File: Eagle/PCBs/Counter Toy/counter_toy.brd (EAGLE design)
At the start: 55.9 x 81.3 mm, 210 parts, among them Q100 2N7002, Q101 2N7002, Q102 2N7002, Q103 2N7002, Q104 2N7002, Q105 2N7002, Q106 2N7002, Q11 2N7002, Q12 2N7002, Q126 2N7002, Q127 2N7002, Q128 2N7002, Q129 2N7002, Q130 2N7002, Q131 2N7002, Q132 2N7002, Q133 2N7002, Q134 2N7002, Q135 2N7002, Q136 2N7002, Q137 2N7002, Q138 2N7002, Q139 2N7002, Q140 2N7002, Q141 2N7002, Q142 2N7002, Q162 2N7002, Q163 2N7002, Q164 2N7002, Q165 2N7002, Q166 2N7002, Q167 2N7002, Q168 2N7002, Q169 2N7002, Q170 2N7002, Q171 2N7002, Q172 2N7002, Q173 2N7002, Q174 2N7002, Q175 2N7002, Q176 2N7002, Q177 2N7002, Q178 2N7002, Q18 2N7002, Q19 2N7002, Q198 2N7002, Q199 2N7002, Q2 2N7002, Q20 2N7002, Q200 2N7002, Q201 2N7002, Q202 2N7002, Q203 2N7002, Q204 2N7002, Q205 2N7002, Q206 2N7002, Q207 2N7002, Q208 2N7002, Q209 2N7002, Q210 2N7002, Q211 2N7002, Q212 2N7002, Q213 2N7002, Q214 2N7002, Q24 2N7002, Q25 2N7002, Q26 2N7002, Q27 2N7002, Q28 2N7002, Q29 2N7002, Q30 2N7002, Q31 2N7002, Q32 2N7002, Q33 2N7002, Q34 2N7002, Q36 2N7002, Q37 2N7002, Q38 2N7002, Q39 2N7002, Q40 2N7002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

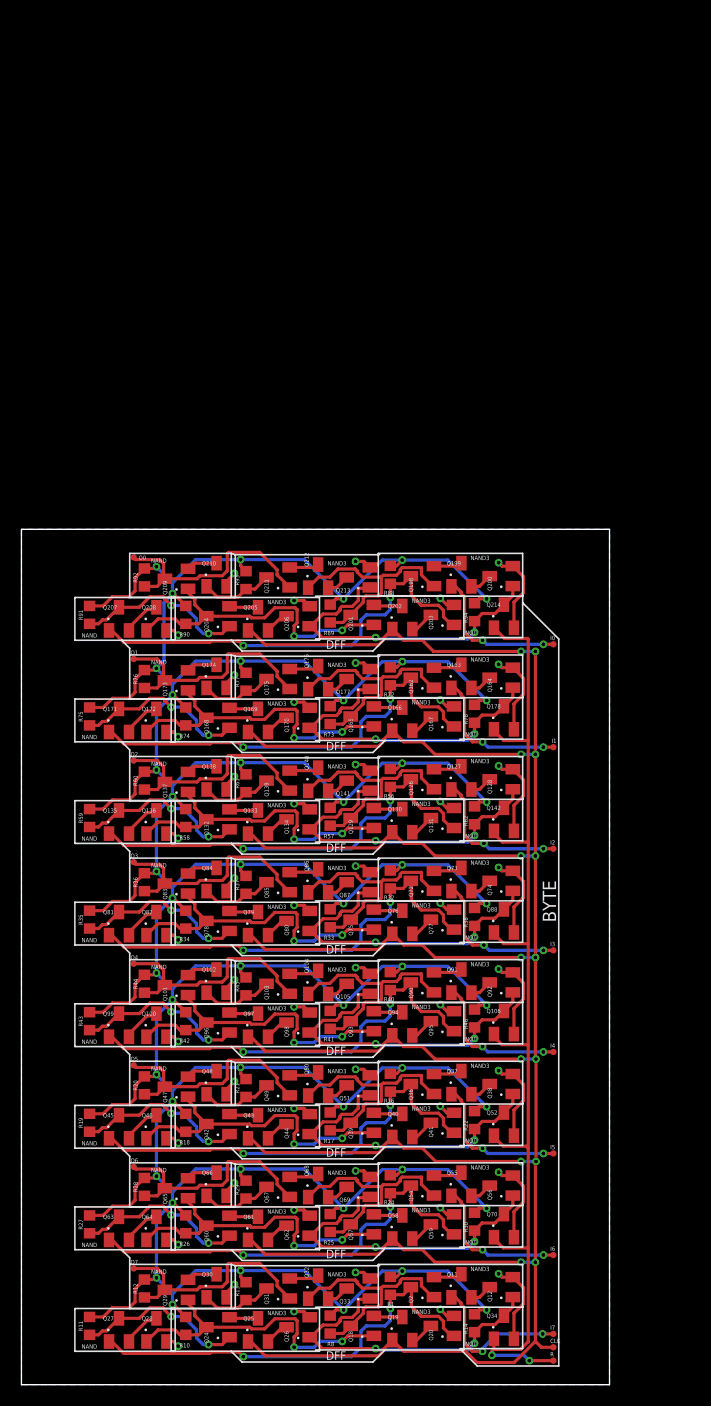
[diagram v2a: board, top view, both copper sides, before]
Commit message: Made a button input and a multiplexer
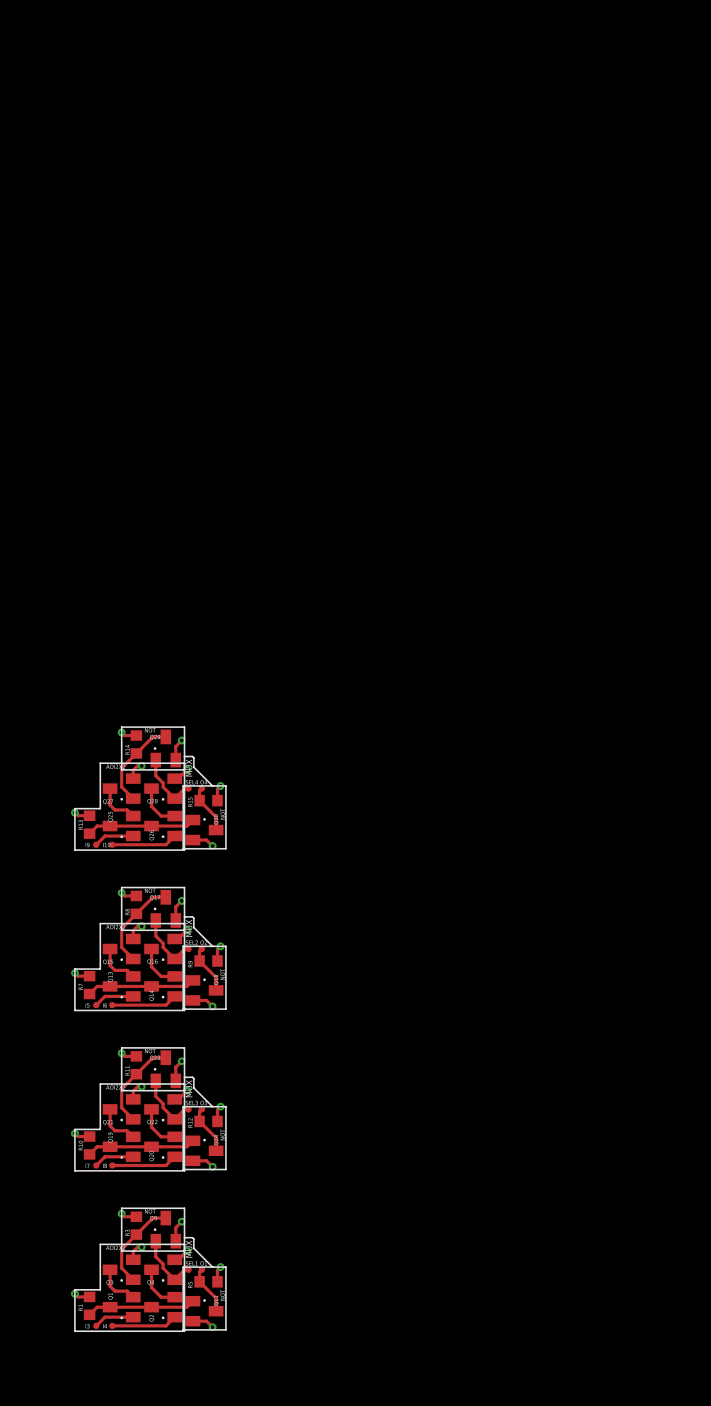
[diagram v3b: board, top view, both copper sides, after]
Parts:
- removed CLK, I0, I1, I2, O0, O5, O6, O7, R: TPPAD6, ellajameson-core:TP06R
- removed Q100, Q101, Q102, Q103, Q104, Q105, Q106, Q12, Q126, Q127, Q128, Q129, Q130, Q131, Q132, Q133, Q134, Q135, Q136, Q137, Q138, Q139, Q140, Q141, Q142, Q162, Q163, Q164, Q165, Q166, Q167, Q168, Q169, Q170, Q171, Q172, Q173, Q174, Q175, Q176, Q177, Q178, Q198, Q199, Q200, Q201, Q202, Q203, Q204, Q205, Q206, Q207, Q208, Q209, Q210, Q211, Q212, Q213, Q214, Q31, Q32, Q33, Q34, Q36, Q37, Q38, Q39, Q40, Q41, Q42, Q43, Q44, Q45, Q46, Q47, Q48, Q49, Q50, Q51, Q52, Q54, Q55, Q56, Q57, Q58, Q59, Q60, Q61, Q62, Q63, Q64, Q65, Q66, Q67, Q68, Q69, Q70, Q72, Q73, Q74, Q75, Q76, Q77, Q78, Q79, Q80, Q81, Q82, Q83, Q84, Q85, Q86, Q87, Q88, Q90, Q91, Q92, Q93, Q94, Q95, Q96, Q97, Q98, Q99: 2N7002, ellajameson-core:SOT23
- removed R16, R17, R18, R19, R20, R21, R22, R24, R25, R26, R27, R28, R29, R30, R32, R33, R34, R35, R36, R37, R38, R40, R41, R42, R43, R44, R45, R46, R56, R57, R58, R59, R60, R61, R62, R72, R73, R74, R75, R76, R77, R78, R88, R89, R90, R91, R92, R93, R94: (no value), ellajameson-core:R0603
- added I10, I8, I9, SEL1, SEL2, SEL3, SEL4: TPPAD6, ellajameson-core:TP06R
- added Q1, Q13, Q14, Q15, Q16, Q17, Q21, Q22, Q23, Q3, Q4, Q9: 2N7002, ellajameson-core:SOT23
- added R15, R3, R5, R7, R9: (no value), ellajameson-core:R0603
- moved R14 63.7 mm to (10.9, 60.8)
- moved O1 58.4 mm to (17.1, 10.9), turned to 270 degrees
- moved I3 56.2 mm to (7.11, 5.59)
- moved Q29 51.4 mm to (13.7, 60.5), turned to 0 degrees
- moved Q28 51.4 mm to (13.5, 56.6), turned to 90 degrees
- moved Q27 51.4 mm to (9.53, 56.6), turned to 90 degrees
- moved Q25 49.6 mm to (9.53, 53.1), turned to 90 degrees
- moved I4 49.3 mm to (8.64, 5.59)
- moved Q26 49.3 mm to (13.5, 53.1)
- moved I6 48.2 mm to (8.64, 36.1)
- moved R13 46.7 mm to (6.48, 53.2)
- moved I7 46.3 mm to (7.11, 20.8)
- moved I5 45.7 mm to (7.11, 36.1)
- moved R8 43.9 mm to (10.9, 45.6)
- moved Q30 43.3 mm to (17.4, 52.7), turned to 270 degrees
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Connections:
- removed net N$10: Q11.3, Q2.2
- removed net N$101: Q104.1, Q90.1, Q93.3, R41.1
- removed net N$102: Q90.3, Q95.1, Q99.1, R40.1
- removed net N$103: I4.TP, Q91.1
- removed net N$104: Q90.2, Q91.3
- removed net N$105: Q91.2, Q92.3
- removed net N$106: Q100.1, Q101.1, Q93.1, Q96.3, R42.1
- removed net N$108: Q93.2, Q94.3
- removed net N$109: Q94.2, Q95.3
- removed net N$11: Q11.2, Q12.3
- removed net N$110: Q96.2, Q97.3
- removed net N$111: Q105.1, Q106.3, Q92.1, Q98.1, R46.1
- removed net N$112: Q97.2, Q98.3
- removed net N$113: Q96.1, Q99.3, R43.1
- removed net N$114: Q100.3, Q99.2
- removed net N$115: Q101.2, Q102.3
- removed net N$116: O4.TP, Q101.3, Q103.1, R44.1
- removed net N$117: Q102.1, Q103.3, R45.1
- removed net N$118: Q103.2, Q104.3
- removed net N$119: Q104.2, Q105.3
- removed net N$14: Q18.1, Q24.3, Q28.1, Q29.1, R10.1
- removed net N$141: Q126.1, Q129.3, Q140.1, R57.1
- removed net N$142: Q126.3, Q131.1, Q135.1, R56.1
- removed net N$143: I2.TP, Q127.1
- removed net N$144: Q126.2, Q127.3
- removed net N$145: Q127.2, Q128.3
- removed net N$146: Q129.1, Q132.3, Q136.1, Q137.1, R58.1
- removed net N$148: Q129.2, Q130.3
- removed net N$149: Q130.2, Q131.3
- removed net N$150: Q132.2, Q133.3
- removed net N$151: Q128.1, Q134.1, Q141.1, Q142.3, R62.1
- removed net N$152: Q133.2, Q134.3
- removed net N$153: Q132.1, Q135.3, R59.1
- removed net N$154: Q135.2, Q136.3
- removed net N$155: Q137.2, Q138.3
- removed net N$156: O2.TP, Q137.3, Q139.1, R60.1
- removed net N$157: Q138.1, Q139.3, R61.1
- removed net N$158: Q139.2, Q140.3
- removed net N$159: Q140.2, Q141.3
- removed net N$181: Q162.1, Q165.3, Q176.1, R73.1
- removed net N$182: Q162.3, Q167.1, Q171.1, R72.1
- removed net N$183: I1.TP, Q163.1
- removed net N$184: Q162.2, Q163.3
- removed net N$185: Q163.2, Q164.3
- removed net N$186: Q165.1, Q168.3, Q172.1, Q173.1, R74.1
- removed net N$188: Q165.2, Q166.3
- removed net N$189: Q166.2, Q167.3
- removed net N$190: Q168.2, Q169.3
- removed net N$191: Q164.1, Q170.1, Q177.1, Q178.3, R78.1
- removed net N$192: Q169.2, Q170.3
- removed net N$193: Q168.1, Q171.3, R75.1
- removed net N$194: Q171.2, Q172.3
- removed net N$195: Q173.2, Q174.3
- removed net N$196: O1.TP, Q173.3, Q175.1, R76.1
- removed net N$197: Q174.1, Q175.3, R77.1
- removed net N$198: Q175.2, Q176.3
- removed net N$199: Q176.2, Q177.3
- removed net N$22: Q24.2, Q25.3
- removed net N$221: Q198.1, Q201.3, Q212.1, R89.1
- removed net N$222: Q198.3, Q203.1, Q207.1, R88.1
- removed net N$223: I0.TP, Q199.1
- removed net N$224: Q198.2, Q199.3
- removed net N$225: Q199.2, Q200.3
- removed net N$226: Q201.1, Q204.3, Q208.1, Q209.1, R90.1
- removed net N$228: Q201.2, Q202.3
- removed net N$229: Q202.2, Q203.3
- removed net N$230: Q204.2, Q205.3
- removed net N$231: Q200.1, Q206.1, Q213.1, Q214.3, R94.1
- removed net N$232: Q205.2, Q206.3
- removed net N$233: Q204.1, Q207.3, R91.1
- removed net N$234: Q207.2, Q208.3
- removed net N$235: Q209.2, Q210.3
- removed net N$236: O0.TP, Q209.3, Q211.1, R92.1
- removed net N$237: Q210.1, Q211.3, R93.1
- removed net N$238: Q211.2, Q212.3
- removed net N$239: Q212.2, Q213.3
- removed net N$41: Q36.1, Q39.3, Q50.1, R17.1
- removed net N$42: Q36.3, Q41.1, Q45.1, R16.1
- removed net N$43: I5.TP, Q37.1
- removed net N$44: Q36.2, Q37.3
- removed net N$45: Q37.2, Q38.3
- removed net N$46: Q39.1, Q42.3, Q46.1, Q47.1, R18.1
- removed net N$48: Q39.2, Q40.3
- removed net N$49: Q40.2, Q41.3
- removed net N$50: Q42.2, Q43.3
- removed net N$51: Q38.1, Q44.1, Q51.1, Q52.3, R22.1
- removed net N$52: Q43.2, Q44.3
- removed net N$53: Q42.1, Q45.3, R19.1
- removed net N$54: Q45.2, Q46.3
- removed net N$55: Q47.2, Q48.3
- removed net N$56: O5.TP, Q47.3, Q49.1, R20.1
- removed net N$57: Q48.1, Q49.3, R21.1
- removed net N$58: Q49.2, Q50.3
- removed net N$59: Q50.2, Q51.3
- removed net N$61: Q54.1, Q57.3, Q68.1, R25.1
- removed net N$62: Q54.3, Q59.1, Q63.1, R24.1
- removed net N$63: I6.TP, Q55.1
- removed net N$64: Q54.2, Q55.3
- removed net N$65: Q55.2, Q56.3
- removed net N$66: Q57.1, Q60.3, Q64.1, Q65.1, R26.1
- removed net N$68: Q57.2, Q58.3
- removed net N$69: Q58.2, Q59.3
- removed net N$70: Q60.2, Q61.3
- removed net N$71: Q56.1, Q62.1, Q69.1, Q70.3, R30.1
- removed net N$72: Q61.2, Q62.3
- removed net N$73: Q60.1, Q63.3, R27.1
- removed net N$74: Q63.2, Q64.3
- removed net N$75: Q65.2, Q66.3
- removed net N$76: O6.TP, Q65.3, Q67.1, R28.1
- removed net N$77: Q66.1, Q67.3, R29.1
- removed net N$78: Q67.2, Q68.3
- removed net N$79: Q68.2, Q69.3
- removed net N$81: Q72.1, Q75.3, Q86.1, R33.1
- removed net N$82: Q72.3, Q77.1, Q81.1, R32.1
- removed net N$83: I3.TP, Q73.1
- removed net N$84: Q72.2, Q73.3
- removed net N$85: Q73.2, Q74.3
- removed net N$86: Q75.1, Q78.3, Q82.1, Q83.1, R34.1
- removed net N$88: Q75.2, Q76.3
- removed net N$89: Q76.2, Q77.3
- removed net N$90: Q78.2, Q79.3
- removed net N$91: Q74.1, Q80.1, Q87.1, Q88.3, R38.1
- removed net N$92: Q79.2, Q80.3
- removed net N$93: Q78.1, Q81.3, R35.1
- removed net N$94: Q81.2, Q82.3
- removed net N$95: Q83.2, Q84.3
- removed net N$96: O3.TP, Q83.3, Q85.1, R36.1
- removed net N$97: Q84.1, Q85.3, R37.1
- removed net N$98: Q85.2, Q86.3
- removed net N$99: Q86.2, Q87.3
- new net N$12: O1.TP, Q11.3, R5.1
- new net N$15: I5.TP, Q13.1
- new net N$16: Q13.3, Q14.3, Q18.1, R7.1
- new net N$2: Q1.3, Q11.1, Q2.3, R1.1
- new net N$20: Q16.1, Q17.1, SEL2.TP
- new net N$28: Q20.2, Q22.3
- new net N$29: Q22.1, Q23.1, SEL3.TP
- new net N$30: I8.TP, Q20.1
- new net N$34: Q25.3, Q26.3, Q30.1, R13.1
- new net N$37: Q28.1, Q29.1, SEL4.TP
- new net N$38: I10.TP, Q26.1
- new net N$39: Q27.1, Q29.3, R14.1
- new net N$40: O4.TP, Q30.3, R15.1
- new net N$5: Q4.1, Q9.1, SEL1.TP
- new net N$6: I4.TP, Q2.1
- new net N$7: Q3.1, Q9.3, R3.1
- net GND: now also Q11.2, Q15.2, Q16.2, Q17.2, Q18.2, Q21.2, Q22.2, Q23.2, Q24.2, Q27.2, Q29.2, Q3.2, Q4.2, Q9.2; no longer Q100.2, Q102.2, Q105.2, Q106.2, Q12.2, Q128.2, Q131.2, Q134.2, Q136.2, Q138.2, Q141.2, Q142.2, Q164.2, Q167.2, Q170.2, Q172.2, Q174.2, Q177.2, Q178.2, Q20.2, Q200.2, Q203.2, Q206.2, Q208.2, Q210.2, Q213.2, Q214.2, Q26.2, Q33.2, Q34.2, Q38.2, Q41.2, Q44.2, Q46.2, Q48.2, Q51.2, Q52.2, Q56.2, Q59.2, Q62.2, Q64.2, Q66.2, Q69.2, Q70.2, Q74.2, Q77.2, Q80.2, Q82.2, Q84.2, Q87.2, Q88.2, Q92.2, Q95.2, Q98.2
- net N$1: now also I3.TP, Q1.1; no longer Q18.3, Q2.1, Q32.1, R8.1
- net N$17: now also Q13.2, Q15.3; no longer CLK.TP, Q130.1, Q133.1, Q166.1, Q169.1, Q19.1, Q202.1, Q205.1, Q25.1, Q40.1, Q43.1, Q58.1, Q61.1, Q76.1, Q79.1, Q94.1, Q97.1
- net N$19: now also Q14.2, Q16.3; no longer Q18.2, Q19.3
- net N$21: now also I6.TP, Q14.1; no longer Q19.2, Q20.3
- net N$23: now also Q15.1, Q17.3, R8.1; no longer Q12.1, Q26.1, Q33.1, Q34.3, R14.1
- net N$24: now also O2.TP, Q18.3, R9.1; no longer Q25.2, Q26.3
- net N$25: now also I7.TP, Q19.1; no longer Q24.1, Q27.3, R11.1
- net N$26: now also Q19.3, Q20.3, Q24.1, R10.1; no longer Q27.2, Q28.3
- net N$27: now also Q19.2, Q21.3; no longer Q29.2, Q30.3
- net N$3: now also Q1.2, Q3.3; no longer Q2.3, Q20.1, Q27.1, R1.1
- net N$31: now also Q21.1, Q23.3, R11.1; no longer O7.TP, Q29.3, Q31.1, R12.1
- net N$32: now also O3.TP, Q24.3, R12.1; no longer Q30.1, Q31.3, R13.1
- net N$33: now also I9.TP, Q25.1; no longer Q31.2, Q32.3
- net N$35: now also Q25.2, Q27.3; no longer Q32.2, Q33.3
- net N$36: now also Q26.2, Q28.3; no longer Q106.1, Q142.1, Q178.1, Q214.1, Q34.1, Q52.1, Q70.1, Q88.1, R.TP
- net N$4: now also Q2.2, Q4.3; no longer I7.TP, Q11.1
- net VCC: now also R15.2, R3.2, R5.2, R7.2, R9.2; no longer R16.2, R17.2, R18.2, R19.2, R20.2, R21.2, R22.2, R24.2, R25.2, R26.2, R27.2, R28.2, R29.2, R30.2, R32.2, R33.2, R34.2, R35.2, R36.2, R37.2, R38.2, R40.2, R41.2, R42.2, R43.2, R44.2, R45.2, R46.2, R56.2, R57.2, R58.2, R59.2, R60.2, R61.2, R62.2, R72.2, R73.2, R74.2, R75.2, R76.2, R77.2, R78.2, R88.2, R89.2, R90.2, R91.2, R92.2, R93.2, R94.2
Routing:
- net VCC: track 489.4 -> 18.2 mm, vias 48 -> 12
- net N$17: track 304.6 -> 4.20 mm, vias 14 -> 0
- net N$36: track 104.5 -> 4.27 mm, vias 2 -> 0
- net GND: track 126.7 -> 30.0 mm, vias 48 -> 16
- net N$222: track 41.9 -> 0.00 mm, vias 2 -> 0
- net N$82: track 41.9 -> 0.00 mm, vias 2 -> 0
- net N$182: track 41.9 -> 0.00 mm, vias 2 -> 0
- net N$62: track 41.9 -> 0.00 mm, vias 2 -> 0
- net N$142: track 41.9 -> 0.00 mm, vias 2 -> 0
- net N$42: track 41.9 -> 0.00 mm, vias 2 -> 0
- net N$102: track 41.9 -> 0.00 mm, vias 2 -> 0
- net N$3: track 41.9 -> 4.20 mm, vias 2 -> 0
- net N$91: track 30.9 -> 0.00 mm, vias 2 -> 0
- net N$151: track 30.9 -> 0.00 mm, vias 2 -> 0
- net N$191: track 30.9 -> 0.00 mm, vias 2 -> 0
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- removed copper zone on layer 16, net GND
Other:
- board outline removed
- board text added: "AOI2X2"
- board text added: "MUX"
- board text removed: "BYTE"
- board text removed: "DFF"
- board text removed: "NAND"
- board text removed: "NAND3"

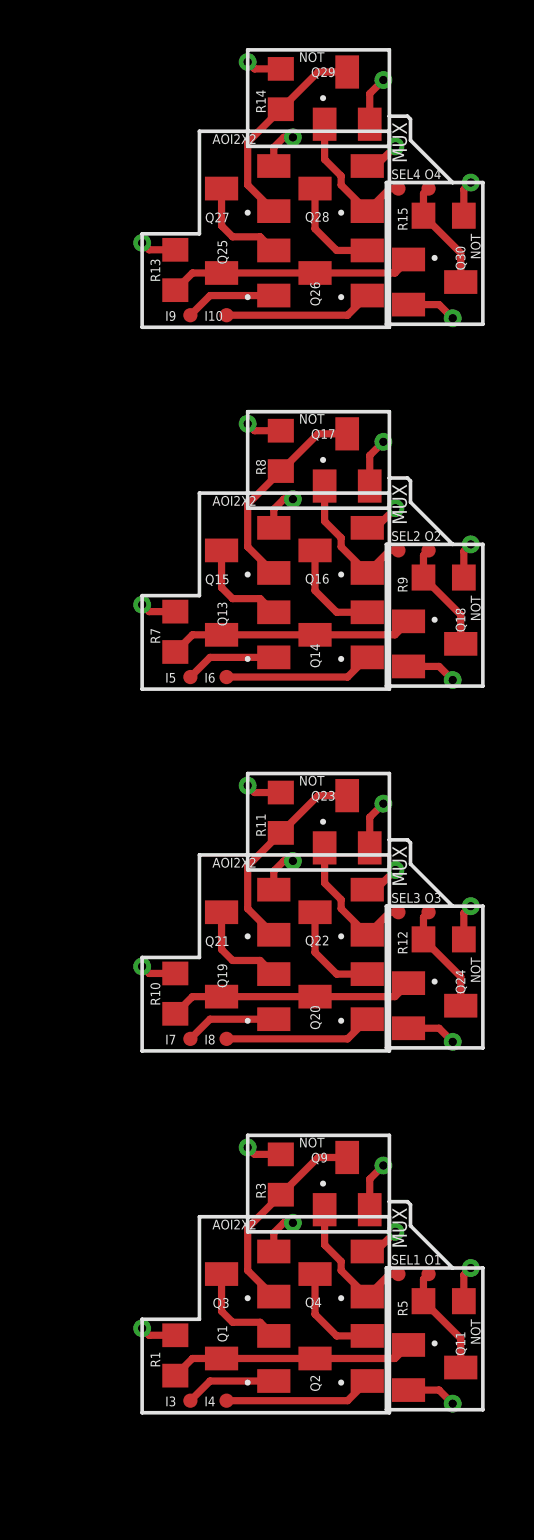
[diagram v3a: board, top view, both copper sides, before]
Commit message: Optimized reset and mux with inversions
No single not gates
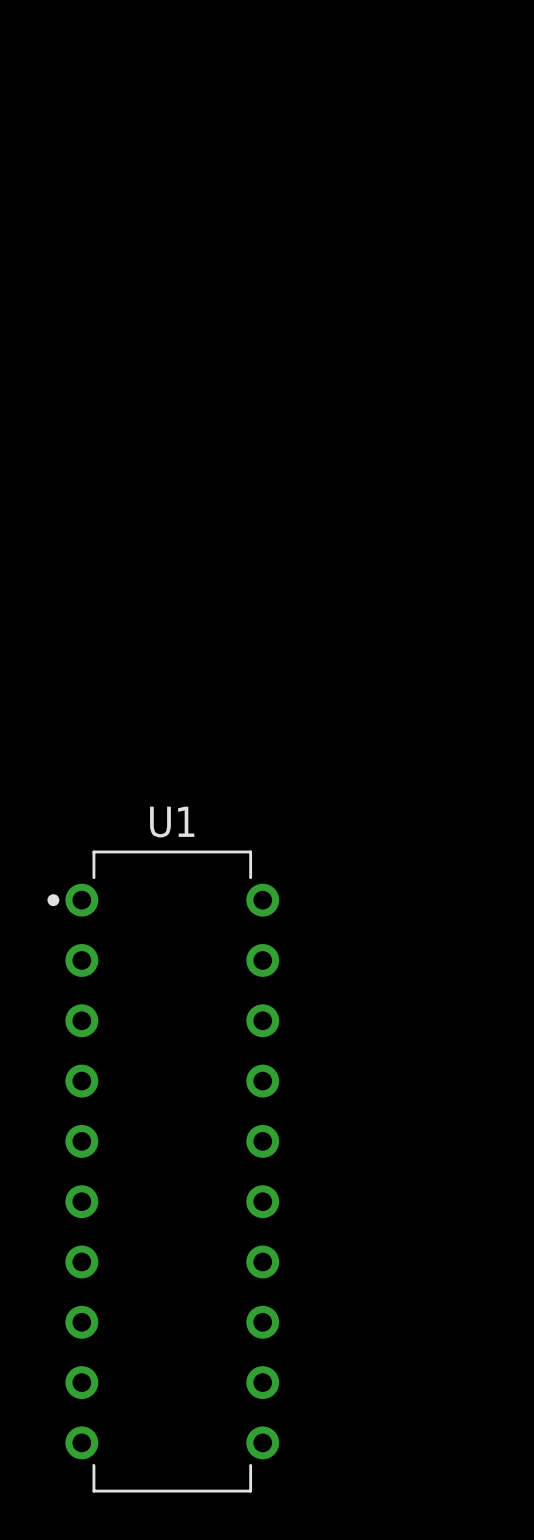
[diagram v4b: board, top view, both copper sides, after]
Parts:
- removed I10, I3, I4, I5, I6, I7, I8, I9, O1, O2, O3, O4, SEL1, SEL2, SEL3, SEL4: TPPAD6, ellajameson-core:TP06R
- removed Q1, Q11, Q13, Q14, Q15, Q16, Q17, Q18, Q19, Q2, Q20, Q21, Q22, Q23, Q24, Q25, Q26, Q27, Q28, Q29, Q3, Q30, Q4, Q9: 2N7002, ellajameson-core:SOT23
- removed R1, R10, R11, R12, R13, R14, R15, R3, R5, R7, R8, R9: (no value), ellajameson-core:R0603
- added U1: SN74S374N, ellajameson-core:DIP762W53P254L2540H508Q20B
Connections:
- removed net N$1: I3.TP, Q1.1
- removed net N$12: O1.TP, Q11.3, R5.1
- removed net N$15: I5.TP, Q13.1
- removed net N$16: Q13.3, Q14.3, Q18.1, R7.1
- removed net N$17: Q13.2, Q15.3
- removed net N$19: Q14.2, Q16.3
- removed net N$2: Q1.3, Q11.1, Q2.3, R1.1
- removed net N$20: Q16.1, Q17.1, SEL2.TP
- removed net N$21: I6.TP, Q14.1
- removed net N$23: Q15.1, Q17.3, R8.1
- removed net N$24: O2.TP, Q18.3, R9.1
- removed net N$25: I7.TP, Q19.1
- removed net N$26: Q19.3, Q20.3, Q24.1, R10.1
- removed net N$27: Q19.2, Q21.3
- removed net N$28: Q20.2, Q22.3
- removed net N$29: Q22.1, Q23.1, SEL3.TP
- removed net N$3: Q1.2, Q3.3
- removed net N$30: I8.TP, Q20.1
- removed net N$31: Q21.1, Q23.3, R11.1
- removed net N$32: O3.TP, Q24.3, R12.1
- removed net N$33: I9.TP, Q25.1
- removed net N$34: Q25.3, Q26.3, Q30.1, R13.1
- removed net N$35: Q25.2, Q27.3
- removed net N$36: Q26.2, Q28.3
- removed net N$37: Q28.1, Q29.1, SEL4.TP
- removed net N$38: I10.TP, Q26.1
- removed net N$39: Q27.1, Q29.3, R14.1
- removed net N$4: Q2.2, Q4.3
- removed net N$40: O4.TP, Q30.3, R15.1
- removed net N$5: Q4.1, Q9.1, SEL1.TP
- removed net N$6: I4.TP, Q2.1
- removed net N$7: Q3.1, Q9.3, R3.1
- net GND: now also U1.10; no longer Q11.2, Q15.2, Q16.2, Q17.2, Q18.2, Q21.2, Q22.2, Q23.2, Q24.2, Q27.2, Q28.2, Q29.2, Q3.2, Q30.2, Q4.2, Q9.2
- net VCC: now also U1.20; no longer R1.2, R10.2, R11.2, R12.2, R13.2, R14.2, R15.2, R3.2, R5.2, R7.2, R8.2, R9.2
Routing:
- net GND: track 30.0 -> 0.00 mm, vias 16 -> 0
- net VCC: track 18.2 -> 0.00 mm, vias 12 -> 0
- net N$34: track 10.4 -> 0.00 mm
- net N$26: track 10.4 -> 0.00 mm
- net N$16: track 10.4 -> 0.00 mm
- net N$2: track 10.4 -> 0.00 mm
- net N$7: track 8.77 -> 0.00 mm
- net N$39: track 8.77 -> 0.00 mm
- net N$31: track 8.77 -> 0.00 mm
- net N$23: track 8.77 -> 0.00 mm
- net N$38: track 6.27 -> 0.00 mm
- net N$21: track 6.27 -> 0.00 mm
- net N$6: track 6.27 -> 0.00 mm
- net N$30: track 6.27 -> 0.00 mm
- net N$20: track 6.11 -> 0.00 mm
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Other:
- board text removed: "AOI2X2"
- board text removed: "MUX"
- board text removed: "NOT"
